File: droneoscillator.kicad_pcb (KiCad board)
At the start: 2 copper layers, 29.5 x 114.3 mm, 48 parts, among them J1 Conn_01x02, J2 Conn_01x03, Q1 BC337, Q2 BC337, Q3 BC337, Q4 BC337, U1 NE5532

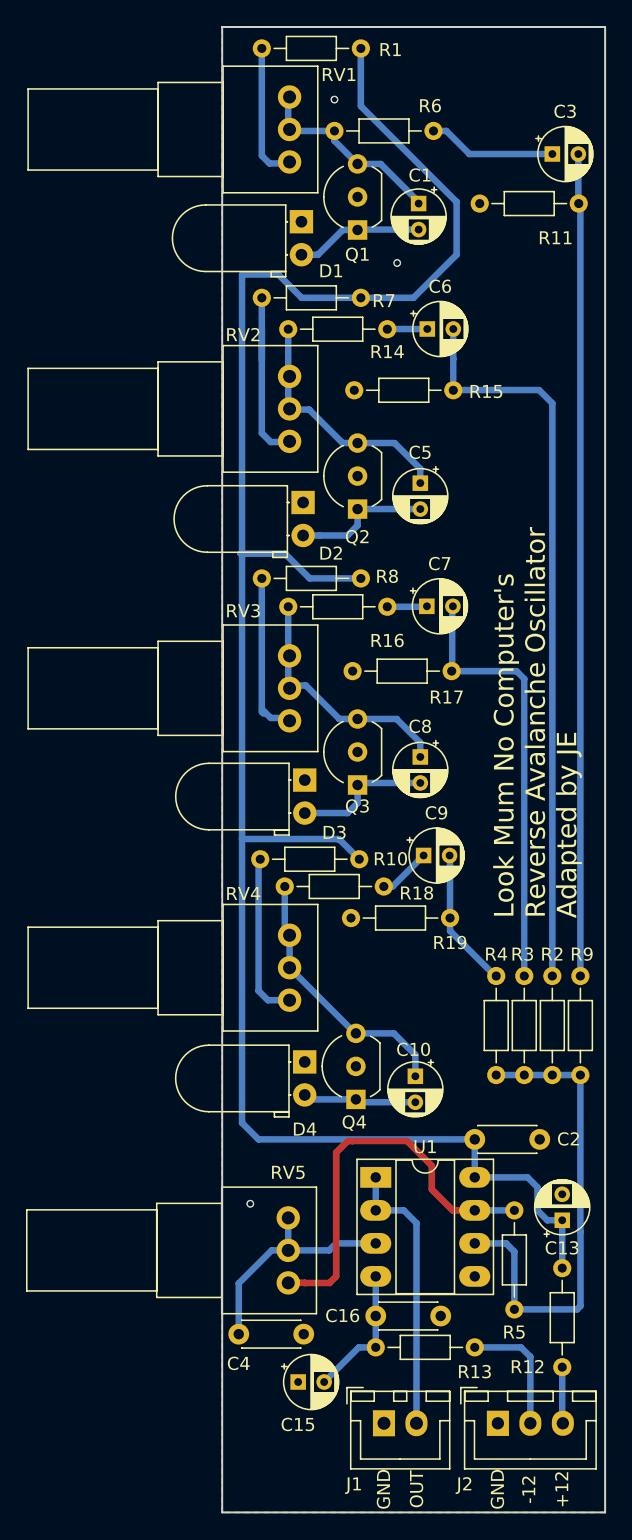
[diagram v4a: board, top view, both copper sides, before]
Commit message: changed PCB dimensions to fit wider range of racks
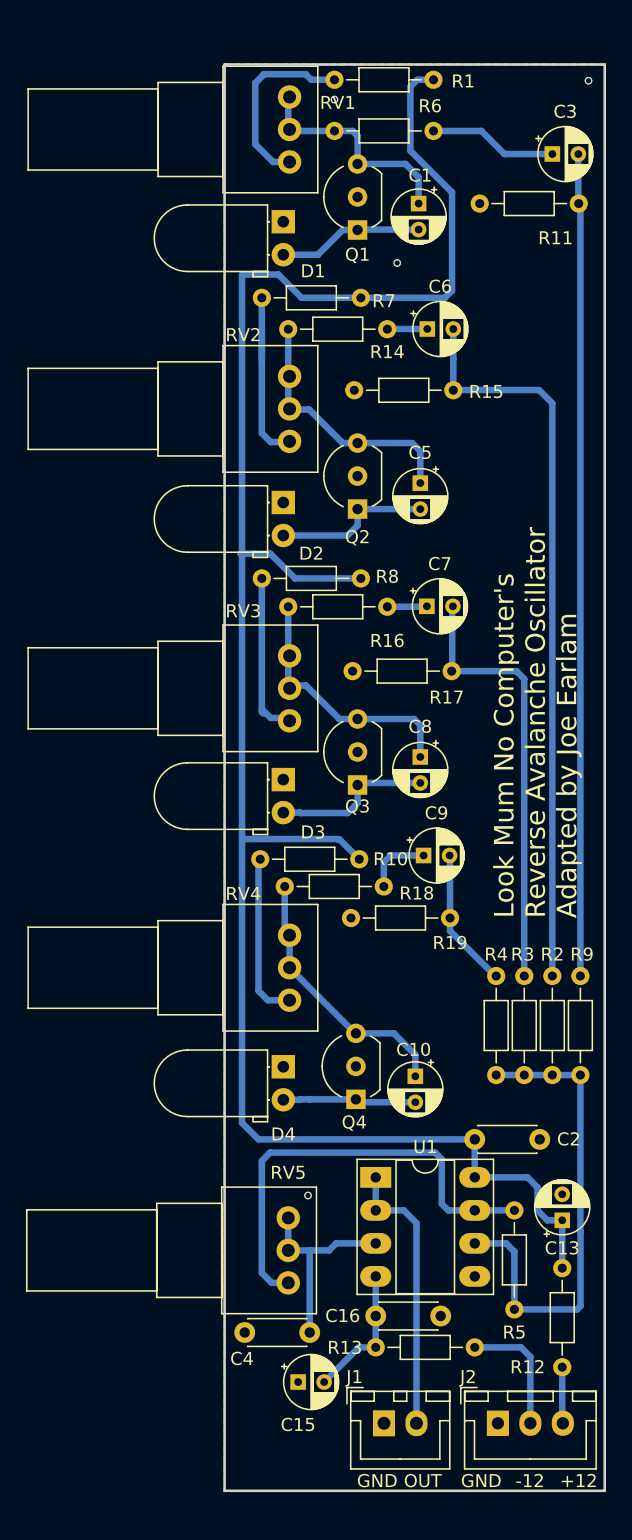
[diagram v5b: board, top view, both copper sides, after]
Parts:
- moved R1 6.09 mm to (147.6, 42.9)
- moved C4 5.46 mm to (138.0, 139.3), turned to 180 degrees
- moved D4 1.69 mm to (136.0, 118.9)
- moved D3 1.65 mm to (136.0, 96.8)
- moved D2 1.52 mm to (136.0, 75.5)
- moved D1 1.40 mm to (136.0, 53.8)
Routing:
- net Net-(R1-Pad2): track 9.83 -> 14.5 mm
- net Net-(R5-Pad1): track 30.8 -> 34.5 mm
- net Net-(C4-Pad1): track 18.2 -> 15.8 mm
- net Net-(C10-Pad2): track 8.22 -> 10.3 mm
- net Net-(C1-Pad1): track 15.4 -> 17.3 mm
- net Net-(C8-Pad2): track 10.7 -> 12.3 mm
- net Net-(C5-Pad2): track 10.6 -> 12.1 mm
- net +12V: track 156.7 -> 155.3 mm
- net Net-(C1-Pad2): track 9.82 -> 11.2 mm
- net Net-(C9-Pad1): track 4.16 -> 5.25 mm
- net Net-(C5-Pad1): track 19.3 -> 20.1 mm
- net Net-(C8-Pad1): track 19.1 -> 19.9 mm
- net GND: vias 3 -> 4
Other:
- board size 29.5 x 114.3 mm -> 29.2 x 109.8 mm
- board text added: "Look Mum No Computer's Reverse Avalanche Oscillator Adapted by Joe Earlam"
- board text removed: "Look Mum No Computer's Reverse Avalanche Oscillator Adapted by JE"

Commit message: small tweaks, ready for sending to production
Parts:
- J1: value Conn_01x02 -> JST_XH_2
- J2: value Conn_01x03 -> JST_XH_3
- moved C4 6.51 mm to (140.0, 133.1), turned to 270 degrees
- moved C15 2.92 mm to (137.2, 146.1)
- moved J1 1.78 mm to (143.8, 144.5)
- moved J2 1.78 mm to (152.5, 144.5)
- moved R12 1.52 mm to (157.5, 132.8)
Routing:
- net Net-(C4-Pad1): track 15.8 -> 9.08 mm
- net -12VA: track 10.5 -> 14.6 mm
- net Net-(C10-Pad1): track 20.5 -> 23.4 mm
- net Net-(J1-Pad2): track 21.5 -> 19.7 mm
- net Net-(J2-Pad2): track 9.70 -> 7.92 mm
- net /OscD: track 10.4 -> 11.9 mm
- net +12V: track 155.3 -> 154.1 mm
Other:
- board size 29.2 x 109.8 mm -> 29.3 x 108.1 mm

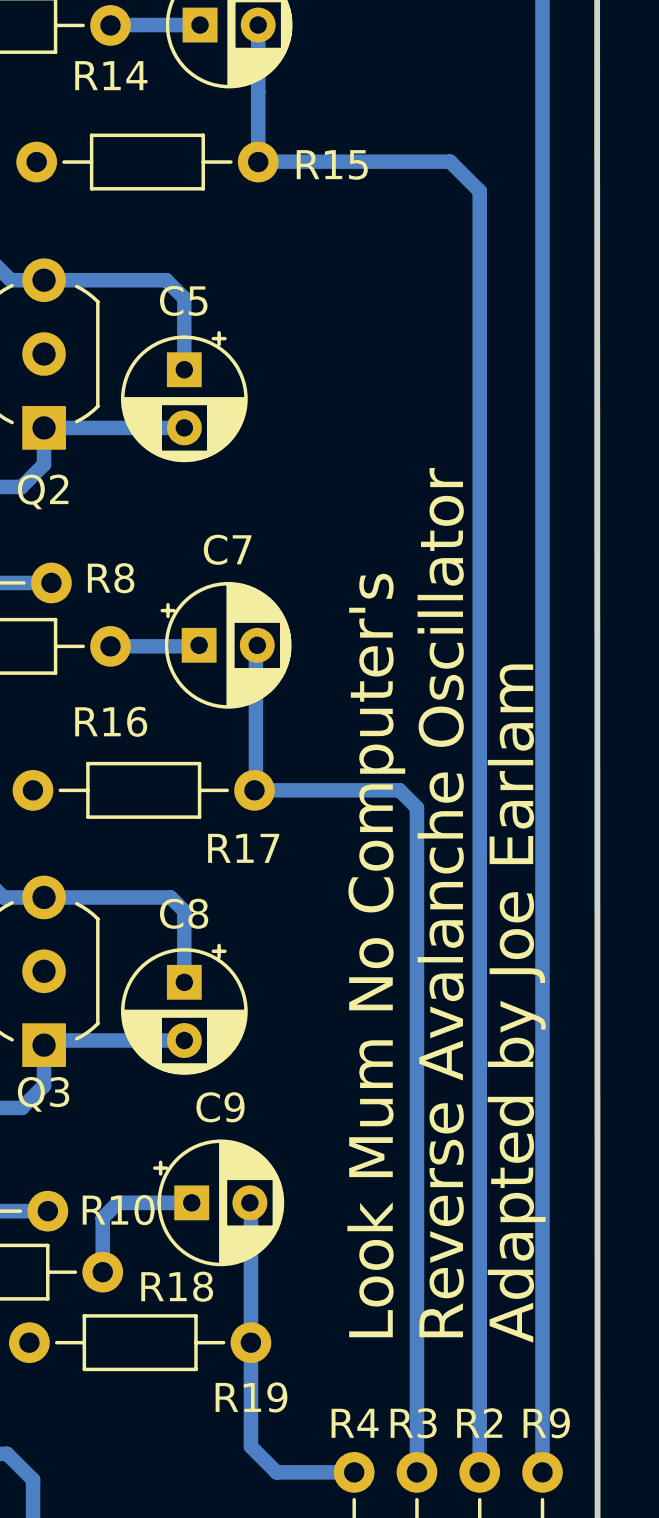
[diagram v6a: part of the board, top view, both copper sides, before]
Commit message: updated front panel hole dimensions
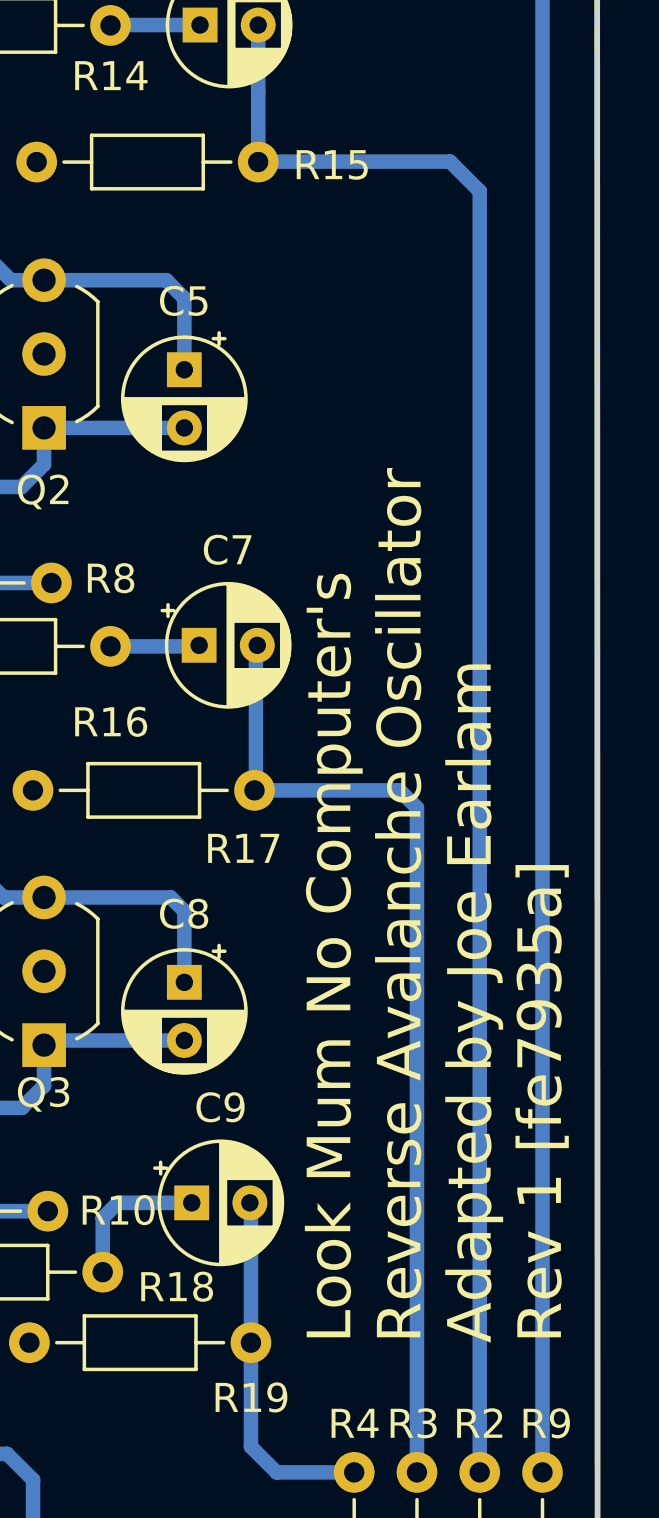
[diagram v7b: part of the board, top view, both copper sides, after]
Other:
- board text added: "Look Mum No Computer's Reverse Avalanche Oscillator Adapted by Joe Earlam Rev 1 [fe7935a]"
- board text removed: "Look Mum No Computer's Reverse Avalanche Oscillator Adapted by Joe Earlam"
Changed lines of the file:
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@@
   )
   (setup
-    (last_trace_width 0.5)
+    (last_trace_width 0.25)
     (user_trace_width 0.5)
     (user_trace_width 0.75)
@@
     (visible_elements 7FFFFFFF)
     (pcbplotparams
-      (layerselection 0x010f0_80000001)
+      (layerselection 0x010f0_ffffffff)
       (usegerberextensions true)
       (usegerberattributes false)
@@
       (drillshape 0)
       (scaleselection 1)
-      (outputdirectory "Gerbers/"))
+      (outputdirectory "../../../../gerbers/LMNC/"))
   )
   (net 0 "")
@@
     (effects (font (size 1 1) (thickness 0.2)))
   )
-  (gr_text "Look Mum No Computer's\nReverse Avalanche Oscillator\nAdapted by Joe Earlam" (at 155.448 107.442 90) (layer F.SilkS)
+  (gr_text "Look Mum No Computer's\nReverse Avalanche Oscillator\nAdapted by Joe Earlam\nRev 1 [fe7935a]" (at 155.194 107.442 90) (layer F.SilkS)
     (effects (font (size 1.5 1.5) (thickness 0.3)) (justify left))
   )

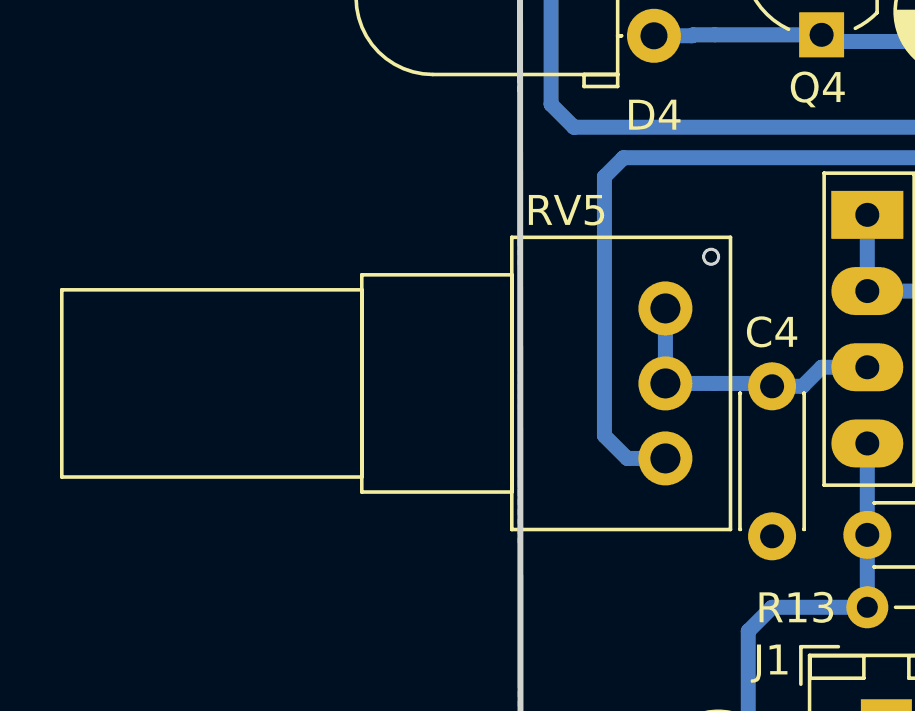
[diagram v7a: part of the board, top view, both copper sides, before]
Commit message: updated front panel hole dimensions
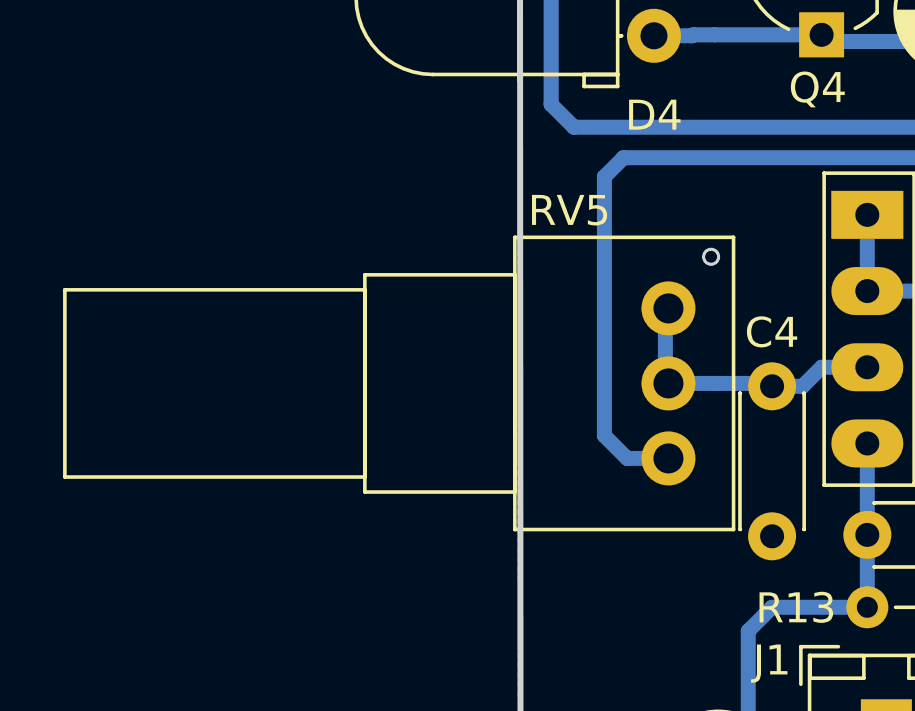
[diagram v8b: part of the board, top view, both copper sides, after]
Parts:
- moved RV5 0.10 mm to (136.5, 130.5)
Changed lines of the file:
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@@
   )
   (module Potentiometer_THT:Potentiometer_Alps_RK097_Single_Horizontal locked (layer F.Cu)
-    (at 136.398 130.5 180)
+    (at 136.5 130.5 180)
     (descr "Potentiometer, horizontal, Alps RK097 Single, http://www.alps.com/prod/info/E/HTML/Potentiometer/RotaryPotentiometers/RK097/RK097_list.html")
     (tags "Potentiometer horizontal Alps RK097 Single")
